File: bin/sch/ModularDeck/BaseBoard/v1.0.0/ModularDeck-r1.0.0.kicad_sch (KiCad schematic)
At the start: 16 parts, among them J3 Conn_01x04, J5 Conn_01x02, J6 Conn_01x04, J7 Conn_01x04, J8 Conn_01x04, U15 STM32F4_Black_Pill, U16 Arduino_Nano_33

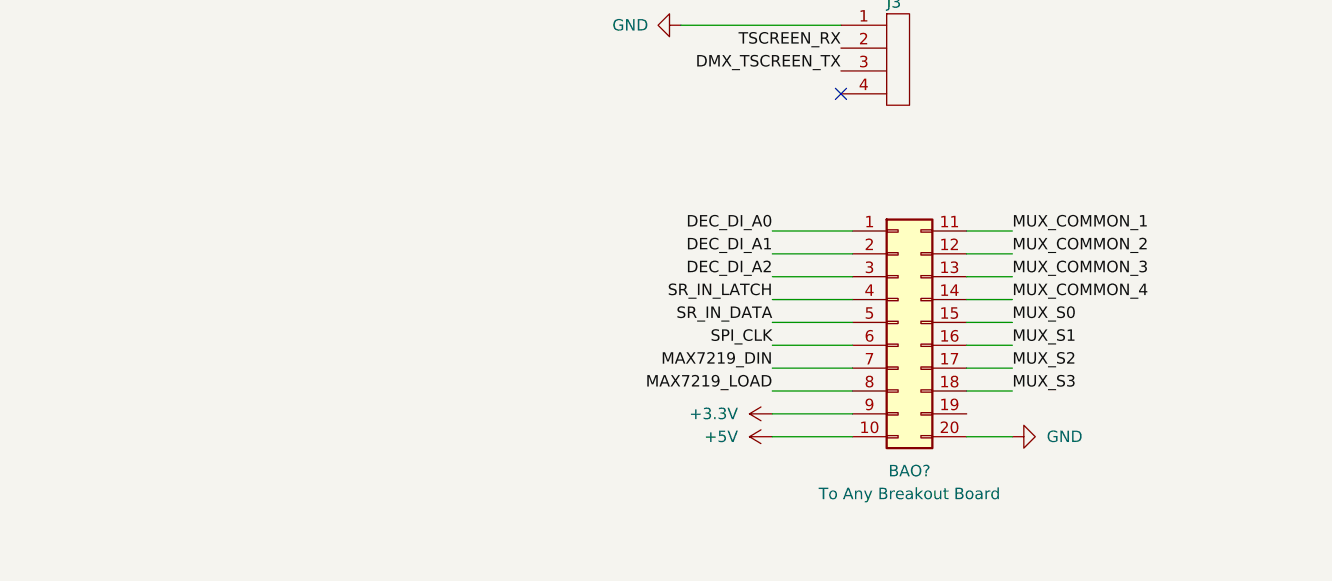
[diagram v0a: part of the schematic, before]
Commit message: Finalised schematics for ModularDeck v1.0.0 (but probably really 0.0.1
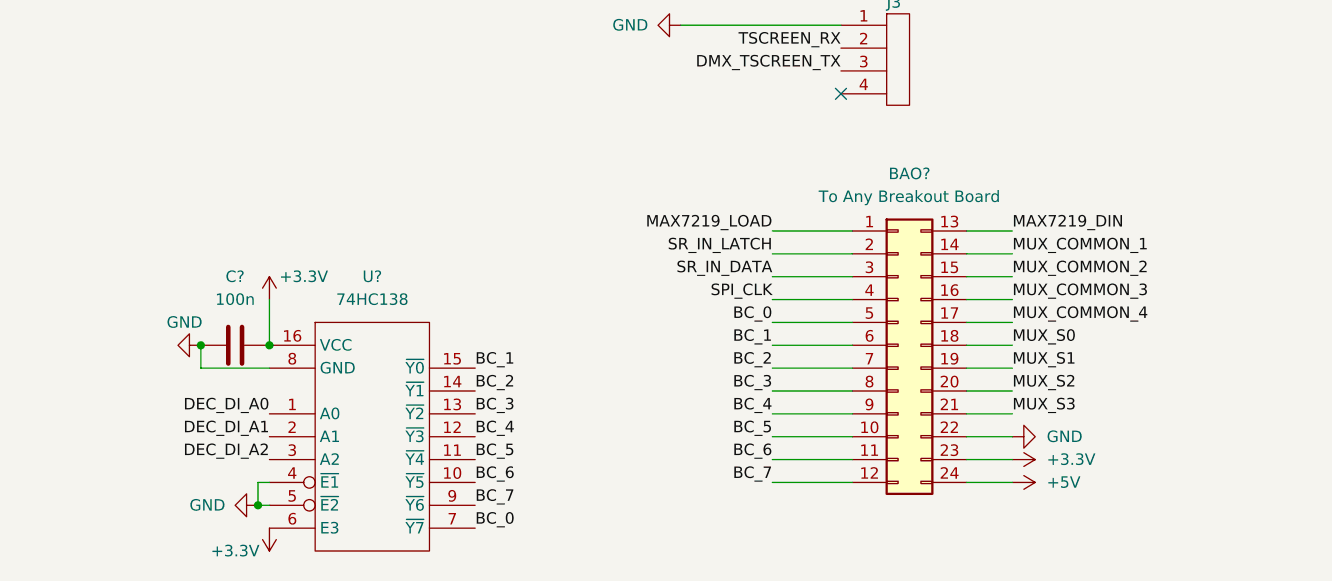
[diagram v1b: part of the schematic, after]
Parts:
- removed BAO?: Conn_02x10_Top_Bottom, symbol Connector_Generic:Conn_02x10_Top_Bottom
- added BAO?: Conn_02x12_Top_Bottom, symbol Connector_Generic:Conn_02x12_Top_Bottom
- added C?: 100n, Capacitor_SMD:C_0402_1005Metric, symbol Device:C
- added U?: 74HC138, Package_SO:SO-16_3.9x9.9mm_P1.27mm, symbol igor_lib:74HC138
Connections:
- net +3V3: now also BAO?.23 (Pin_23), C?.2, U?.16 (VCC), U?.6 (E3)
- net +5V: now also BAO?.24 (Pin_24)
- net DEC_DI_A0: now also U?.1 (A0)
- net DEC_DI_A1: now also U?.2 (A1)
- net DEC_DI_A2: now also U?.3 (A2)
- net GND: now also BAO?.22 (Pin_22), C?.1, U?.4 (~{E1}), U?.5 (~{E2}), U?.8 (GND)
- net MAX7219_DIN: now also BAO?.13 (Pin_13)
- net MAX7219_LOAD: now also BAO?.1 (Pin_1)
- net MUX_COMMON_1: now also BAO?.14 (Pin_14)
- net MUX_COMMON_2: now also BAO?.15 (Pin_15)
- net MUX_COMMON_3: now also BAO?.16 (Pin_16)
- net MUX_COMMON_4: now also BAO?.17 (Pin_17)
- net MUX_S0: now also BAO?.18 (Pin_18)
- net MUX_S1: now also BAO?.19 (Pin_19)
- net MUX_S2: now also BAO?.20 (Pin_20)
- net MUX_S3: now also BAO?.21 (Pin_21)
- net SPI_CLK: now also BAO?.4 (Pin_4)
- net SR_IN_DATA: now also BAO?.3 (Pin_3)
- net SR_IN_LATCH: now also BAO?.2 (Pin_2)
- new net BC_0: BAO?.5 (Pin_5), U?.7 (~{Y7})
- new net BC_1: BAO?.6 (Pin_6), U?.15 (~{Y0})
- new net BC_2: BAO?.7 (Pin_7), U?.14 (~{Y1})
- new net BC_3: BAO?.8 (Pin_8), U?.13 (~{Y2})
- new net BC_4: BAO?.9 (Pin_9), U?.12 (~{Y3})
- new net BC_5: BAO?.10 (Pin_10), U?.11 (~{Y4})
- new net BC_6: BAO?.11 (Pin_11), U?.10 (~{Y5})
- new net BC_7: BAO?.12 (Pin_12), U?.9 (~{Y6})

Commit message: Final changes to 0.0.4 before redoing for 0.1.1
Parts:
- removed BAO?: Conn_02x12_Top_Bottom, symbol Connector_Generic:Conn_02x12_Top_Bottom
- added BAO1: Conn_02x12_Odd_Even, Connector_PinHeader_2.54mm:PinHeader_2x12_P2.54mm_Vertical, symbol Connector_Generic:Conn_02x12_Odd_Even
- gave numbers to parts that had none: 4
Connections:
- net +3V3: now also BAO1.12 (Pin_12)
- net +5V: now also BAO1.9 (Pin_9)
- net BC_0: now also BAO1.7 (Pin_7)
- net BC_1: now also BAO1.8 (Pin_8)
- net BC_2: now also BAO1.5 (Pin_5)
- net BC_3: now also BAO1.6 (Pin_6)
- net BC_4: now also BAO1.3 (Pin_3)
- net BC_5: now also BAO1.4 (Pin_4)
- net BC_6: now also BAO1.1 (Pin_1)
- net BC_7: now also BAO1.2 (Pin_2)
- net GND: now also BAO1.10 (Pin_10)
- net MAX7219_DIN: now also BAO1.16 (Pin_16)
- net MAX7219_LOAD: now also BAO1.15 (Pin_15)
- net MUX_COMMON_1: now also BAO1.17 (Pin_17)
- net MUX_COMMON_2: now also BAO1.19 (Pin_19)
- net MUX_COMMON_3: now also BAO1.21 (Pin_21)
- net MUX_COMMON_4: now also BAO1.23 (Pin_23)
- net MUX_S0: now also BAO1.18 (Pin_18)
- net MUX_S1: now also BAO1.20 (Pin_20)
- net MUX_S2: now also BAO1.22 (Pin_22)
- net MUX_S3: now also BAO1.24 (Pin_24)
- net SPI_CLK: now also BAO1.11 (Pin_11)
- net SR_IN_DATA: now also BAO1.13 (Pin_13)
- net SR_IN_LATCH: now also BAO1.14 (Pin_14)
- net (USB_D-): now reaches U15.8 (A11/USB_D-)
- net (USB_D+): now reaches U15.9 (A12/USB_D+)
- no-connect marks 18 -> 16
